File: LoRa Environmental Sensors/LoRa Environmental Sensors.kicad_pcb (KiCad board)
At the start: 2 copper layers, 8 parts, among them U1 BME280, U2 ATtiny85-20SU, U3 RFM95W-868S2

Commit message: update hardware
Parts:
- added J1: SPI, Connector_PinHeader_2.54mm:PinHeader_2x03_P2.54mm_Vertical, B.Cu at (165.7, 55.9)
- C1, C2: value C -> 0.1uF
- moved R2 11.4 mm to (160.7, 57.1)
- moved C1 11.3 mm to (155.6, 64.1)
- moved U2 5.08 mm to (167.6, 66.0)
- moved C2 4.84 mm to (158.8, 63.7)
- moved U1 4.58 mm to (156.2, 57.1)
- moved R1 4.16 mm to (160.0, 69.8), turned to 0 degrees
- moved BT1 0.64 mm to (163.8, 74.3)
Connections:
- net +3V3 renamed VCC
- R1 pad 1: /SCK -> /CS
- R2 pad 1: /CS -> /NSS
- U2 pad 1: Net-(U2-Pad1) -> /AtTiny_Reset

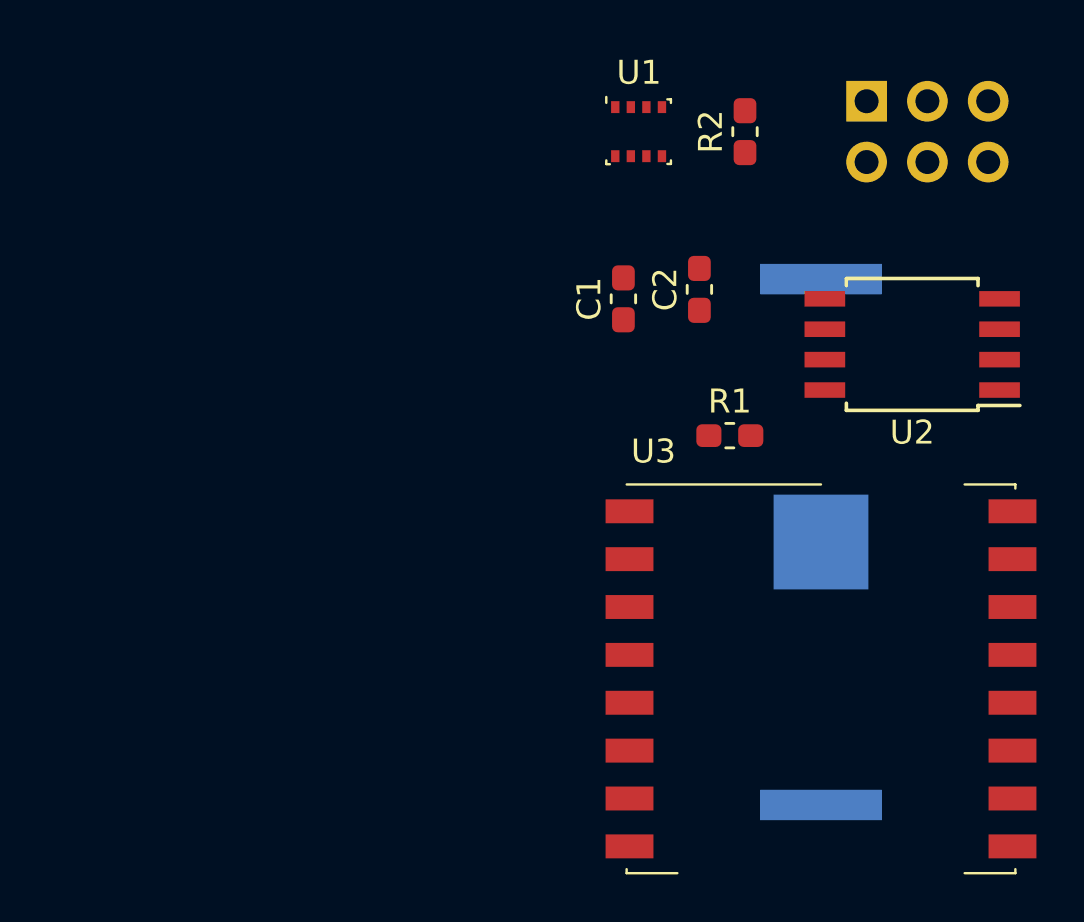
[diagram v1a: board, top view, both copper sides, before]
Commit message: update env sensor
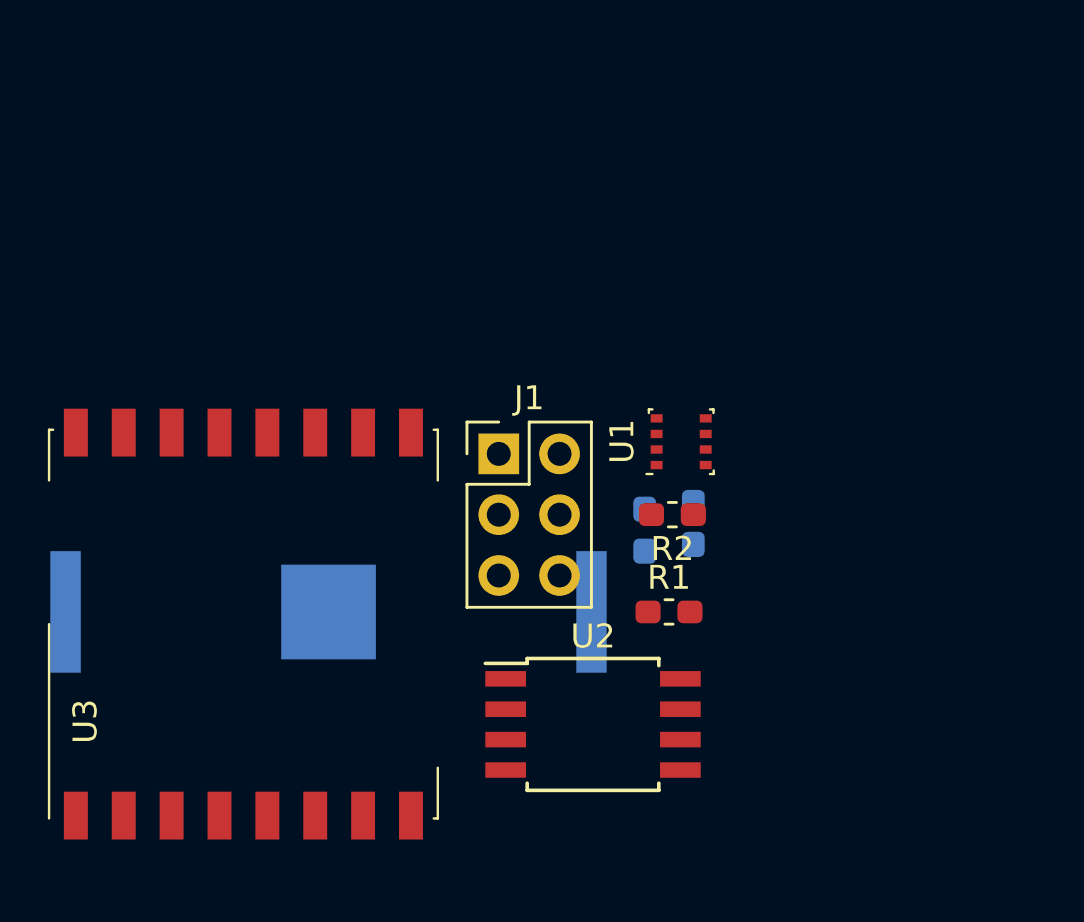
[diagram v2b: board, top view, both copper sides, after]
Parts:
- C1, C2: moved to B.Cu
- J1: moved to F.Cu
- moved U3 24.2 mm to (139.7, 77.7), turned to 90 degrees
- moved J1 21.3 mm to (150.4, 70.6), turned to 0 degrees
- moved BT1 20.8 mm to (143.3, 77.2), turned to 0 degrees
- moved U2 20.7 mm to (154.3, 81.9), turned to 0 degrees
- moved R2 16.3 mm to (157.6, 73.2), turned to 180 degrees
- moved U1 13.1 mm to (158.0, 70.1), turned to 90 degrees
- moved C2 9.78 mm to (158.5, 73.5), turned to 270 degrees
- moved C1 9.71 mm to (156.5, 73.8), turned to 270 degrees
- moved R1 7.79 mm to (157.5, 77.2)
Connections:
- U1 pad 5: /MOSI -> /MISO
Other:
- net class Default: clearance 0.2 -> 0.254; trace_width 0.25 -> 0.254; via_dia 0.8 -> 0.762; via_drill 0.4 -> 0.381
- rule pad_to_mask_clearance: 0.2 -> 0.0508
- rule trace_clearance: 0.2 -> 0.254
- rule trace_min: 0.2 -> 0.1524
- rule via_min_drill: 0.3 -> 0.3302
- rule via_min_size: 0.4 -> 0.6858
